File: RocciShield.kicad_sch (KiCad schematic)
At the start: 188 parts, among them J1 Battery, J10 M2, J11 I2C6, J12 Power, J13 M3, J14 I2C7, J2 I2C0, J3 I2C1, J4 I2C2, J5 I2C3, J6 M0, J7 I2C4, J8 M1, J9 I2C5, Q1 IRF7404, Q2 2N7002, U1 LMR33630, U2 LM317_TO-252, U3 LM317_TO-252, U4 TPS3700, U5 TCA9548A, U6 DRV8871, U7 DRV8871, U8 DRV8871, U9 DRV8871

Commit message: first finished routing. Needs some cleanup
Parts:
- C4, C5: LCSC C3009395 -> C212716; LSCL C3009395 -> (none)
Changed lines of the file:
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@@
       (effects (font (size 1.27 1.27)) hide)
     )
-    (property "LSCL" "C3009395" (at 386.08 54.61 0)
-      (effects (font (size 1.27 1.27)) hide)
-    )
-    (property "LCSC" "C3009395" (at 387.35 49.53 0)
+    (property "LCSC" "C212716" (at 387.35 49.53 0)
       (effects (font (size 1.27 1.27)) hide)
     )
@@
       (effects (font (size 1.27 1.27)) hide)
     )
-    (property "LSCL" "C3009395" (at 397.51 54.61 0)
-      (effects (font (size 1.27 1.27)) hide)
-    )
-    (property "LCSC" "C3009395" (at 397.51 49.53 0)
+    (property "LCSC" "C212716" (at 397.51 49.53 0)
       (effects (font (size 1.27 1.27)) hide)
     )

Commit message: finsihed routing again
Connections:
- net +12V: no longer J12.1 (Pin_1)
- net +12VA: now also J12.1 (Pin_1)
- net GND: now also J11.2 (Pin_2), J14.2 (Pin_2), J2.2 (Pin_2), J3.2 (Pin_2), J4.2 (Pin_2), J5.2 (Pin_2), J7.2 (Pin_2), J9.2 (Pin_2); no longer J11.1 (Pin_1), J14.1 (Pin_1), J2.1 (Pin_1), J3.1 (Pin_1), J4.1 (Pin_1), J5.1 (Pin_1), J7.1 (Pin_1), J9.1 (Pin_1)
- net at R41.2: now also J7.1 (Pin_1); no longer J7.2 (Pin_2)
- net at R64.2: now also J14.1 (Pin_1); no longer J14.2 (Pin_2)
- net at R4.2: now also J2.1 (Pin_1); no longer J2.2 (Pin_2)
- net at R28.2: now also J4.1 (Pin_1); no longer J4.2 (Pin_2)
- net at R50.2: now also J9.1 (Pin_1); no longer J9.2 (Pin_2)
- net at R34.2: now also J5.1 (Pin_1); no longer J5.2 (Pin_2)
- net at R57.2: now also J11.1 (Pin_1); no longer J11.2 (Pin_2)
- net at R15.2: now also J3.1 (Pin_1); no longer J3.2 (Pin_2)
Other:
- moved on the sheet: C1, C2, C21, C3, C4, C5, C7, L1, R5, R6, R7, TP1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

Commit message: finished silcreen and 3d files
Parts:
- added C22, C23: 100n, Capacitor_SMD:C_0603_1608Metric, symbol Device:C
- added R66: 240, Resistor_SMD:R_0603_1608Metric, symbol Device:R
- added R67: 720, Resistor_SMD:R_0603_1608Metric, symbol Device:R
- added U10: LM317_TO-252, Package_TO_SOT_SMD:TO-252-2, symbol Regulator_Linear:LM317_TO-252
- J10: value M2 -> M3
- J13: value M3 -> M2
- JP6: value A0 -> A1
- JP7: value A0 -> A2
- XA1: footprint PCM_arduino-library:Arduino_Mega2560_Shield -> PCM_arduino-library:Arduino_Mega2560_custom_Shield
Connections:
- net +12VA: now also C22.1, U10.3 (VI)
- net +5V: now also C23.1, R66.2, U10.2 (VO)
- net GND: now also C22.2, C23.2, R67.1
- net M2_IN1: now also TP21.1, U9.3 (IN1), XA1.D10; no longer TP19.1, U8.3 (IN1), XA1.D12
- net M2_IN2: now also TP22.1, U9.2 (IN2), XA1.D9; no longer TP20.1, U8.2 (IN2), XA1.D11
- net M3_IN1: now also TP19.1, U8.3 (IN1), XA1.D12; no longer TP21.1, U9.3 (IN1), XA1.D10
- net M3_IN2: now also TP20.1, U8.2 (IN2), XA1.D11; no longer TP22.1, U9.2 (IN2), XA1.D9
- net PM2_1: now also J13.2 (Pin_2), R58.1, R59.1, U9.6 (OUT1); no longer J10.2 (Pin_2), R51.1, R52.1, U8.6 (OUT1)
- net PM2_2: now also D28.2 (A), D29.1 (K), J13.1 (Pin_1), U9.8 (OUT2); no longer D22.2 (A), D23.1 (K), J10.1 (Pin_1), U8.8 (OUT2)
- net PM3_1: now also J10.2 (Pin_2), R51.1, R52.1, U8.6 (OUT1); no longer J13.2 (Pin_2), R58.1, R59.1, U9.6 (OUT1)
- net PM3_2: now also D22.2 (A), D23.1 (K), J10.1 (Pin_1), U8.8 (OUT2); no longer D28.2 (A), D29.1 (K), J13.1 (Pin_1), U9.8 (OUT2)
- net A2: now reaches JP5.2 (C), U5.21 (A2)
- net A0: now reaches JP7.2 (C), U5.1 (A0)
- net A1: now reaches JP6.2 (C), U5.2 (A1)
- new net: R66.1, R67.2, U10.1 (ADJ)
- no-connect marks 71 -> 65
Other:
- note removed: "TODO: - is the power connector large enough? - do we need max motor current? - what kind of fuse should we use - motor from 0-3 instead of 1-4"

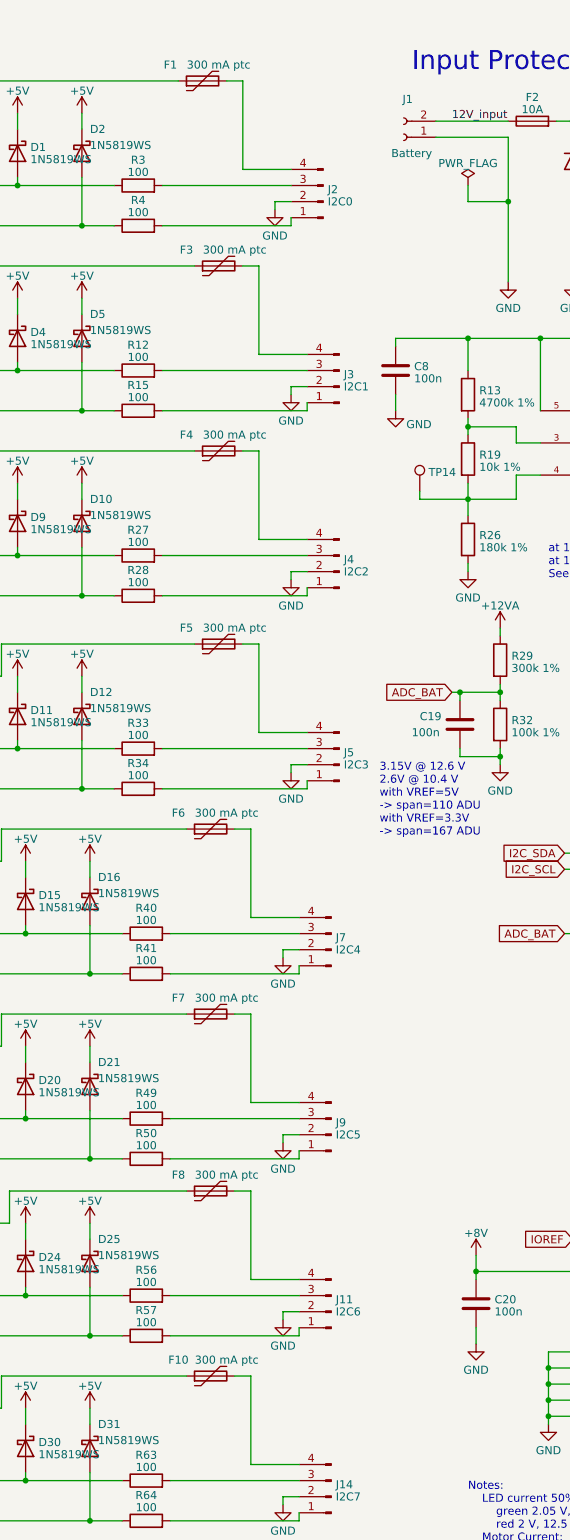
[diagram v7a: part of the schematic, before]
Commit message: changed i2c order
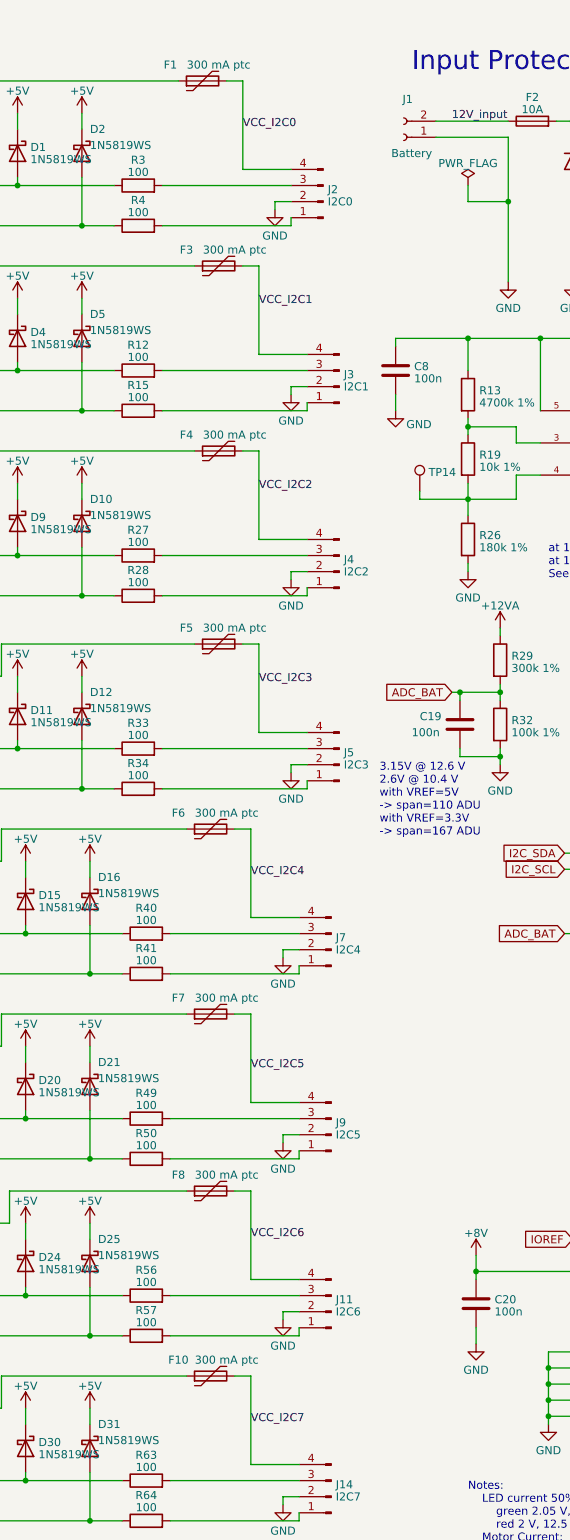
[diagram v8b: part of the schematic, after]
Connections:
- net VCC_I2C7: now reaches F10.2, J14.4 (Pin_4)
- net VCC_I2C0: now reaches F1.2, J2.4 (Pin_4)
- net VCC_I2C3: now reaches F5.2, J5.4 (Pin_4)
- net VCC_I2C2: now reaches F4.2, J4.4 (Pin_4)
- net VCC_I2C6: now reaches F8.2, J11.4 (Pin_4)
- net VCC_I2C4: now reaches F6.2, J7.4 (Pin_4)
- net VCC_I2C1: now reaches F3.2, J3.4 (Pin_4)
- net VCC_I2C5: now reaches F7.2, J9.4 (Pin_4)
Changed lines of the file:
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@@
+    (effects (font (size 1.27 1.27)) (justify left bottom))
+  )
+  (label "VCC_I2C6" (at 168.91 210.82 0) (fields_autoplaced)
     (effects (font (size 1.27 1.27)) (justify left bottom))
   )
@@
     (effects (font (size 1.27 1.27)) (justify left bottom))
   )
+  (label "VCC_I2C4" (at 168.91 153.67 0) (fields_autoplaced)
+    (effects (font (size 1.27 1.27)) (justify left bottom))
+  )
   (label "FB" (at 341.63 36.83 0) (fields_autoplaced)
     (effects (font (size 1.27 1.27)) (justify left bottom))
   )
   (label "A2" (at 46.99 99.06 0) (fields_autoplaced)
+    (effects (font (size 1.27 1.27)) (justify left bottom))
+  )
+  (label "VCC_I2C0" (at 167.64 35.56 0) (fields_autoplaced)
+    (effects (font (size 1.27 1.27)) (justify left bottom))
+  )
+  (label "VCC_I2C3" (at 170.18 123.19 0) (fields_autoplaced)
     (effects (font (size 1.27 1.27)) (justify left bottom))
   )
@@
     (effects (font (size 1.27 1.27)) (justify left bottom))
   )
+  (label "VCC_I2C1" (at 170.18 63.5 0) (fields_autoplaced)
+    (effects (font (size 1.27 1.27)) (justify left bottom))
+  )
   (label "PM1_2" (at 345.44 170.18 0) (fields_autoplaced)
     (effects (font (size 1.27 1.27)) (justify left bottom))
   )
+  (label "VCC_I2C5" (at 168.91 184.15 0) (fields_autoplaced)
+    (effects (font (size 1.27 1.27)) (justify left bottom))
+  )
   (label "PM3_1" (at 345.44 198.12 0) (fields_autoplaced)
+    (effects (font (size 1.27 1.27)) (justify left bottom))
+  )
+  (label "VCC_I2C7" (at 168.91 240.03 0) (fields_autoplaced)
     (effects (font (size 1.27 1.27)) (justify left bottom))
   )
@@
     (effects (font (size 1.27 1.27)) (justify left bottom))
   )
+  (label "VCC_I2C2" (at 170.18 92.71 0) (fields_autoplaced)
+    (effects (font (size 1.27 1.27)) (justify left bottom))
+  )
